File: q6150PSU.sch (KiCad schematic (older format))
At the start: 22 parts, among them P1 Vin, P2 Vout, Q1 Q_NMOS_GSD, T1 TRANSFO, U1 LM3478

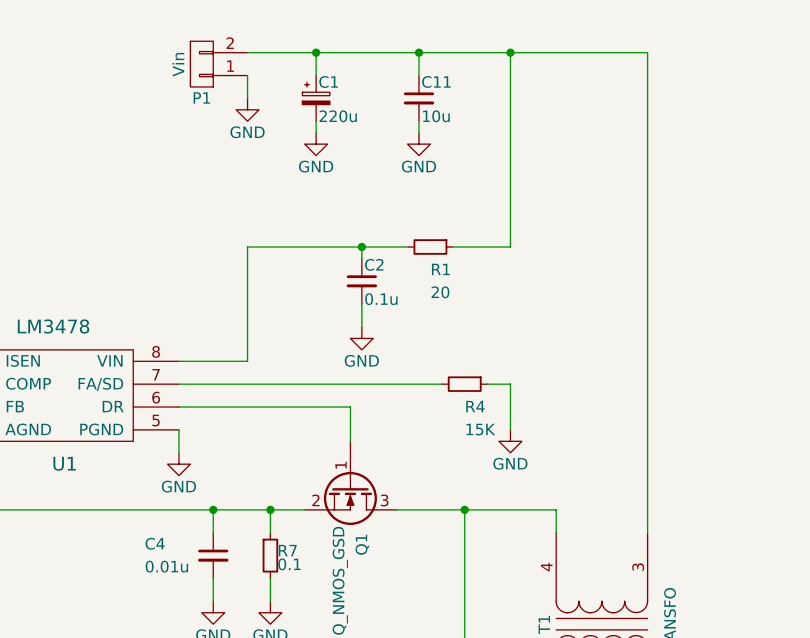
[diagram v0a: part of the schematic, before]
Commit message: All layout + Pot
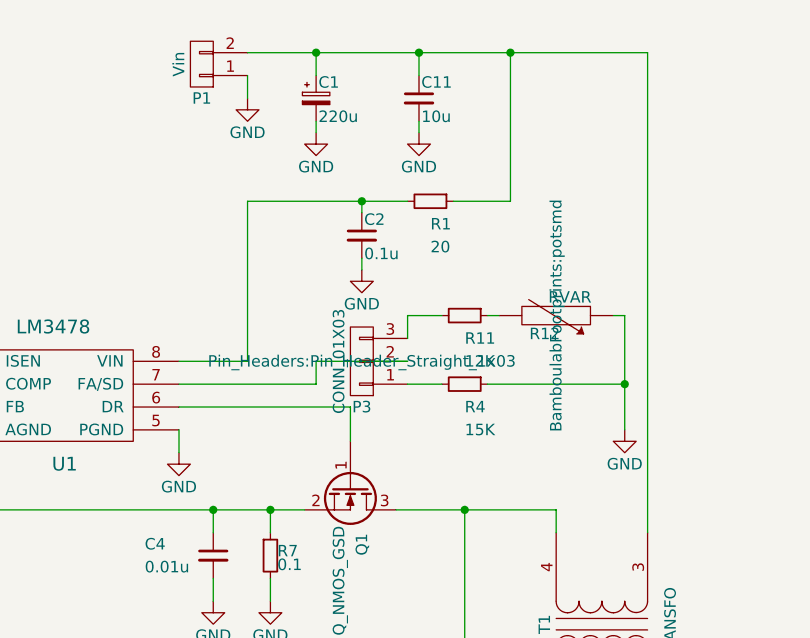
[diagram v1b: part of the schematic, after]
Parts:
- added P3: CONN_01X03, Pin_Headers:Pin_Header_Straight_1x03, symbol CONN_01X03
- added R11: 12K, Resistors_SMD:R_0805_HandSoldering, symbol R_Small
- added R12: RVAR, BamboulabFootprints:potsmd, symbol RVAR
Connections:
- net GND: now also R12.1
- net at U1.7 (FA/SD): now also P3.2 (P2); no longer R4.2
- new net: P3.1 (P1), R4.2
- new net: R11.1, R12.2
- new net: P3.3 (P3), R11.2
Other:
- moved on the sheet: C2, R1
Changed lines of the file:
@@
 L R_Small R1
 U 1 1 57F6A221
-P 5200 2750
-F 0 "R1" V 5300 2750 50  0000 L CNN
-F 1 "20" V 5400 2750 50  0000 L CNN
-F 2 "Resistors_SMD:R_0805_HandSoldering" H 5200 2750 50  0001 C CNN
-F 3 "" H 5200 2750 50  0000 C CNN
-	1    5200 2750
+P 5200 2550
+F 0 "R1" V 5300 2550 50  0000 L CNN
+F 1 "20" V 5400 2550 50  0000 L CNN
+F 2 "Resistors_SMD:R_0805_HandSoldering" H 5200 2550 50  0001 C CNN
+F 3 "" H 5200 2550 50  0000 C CNN
+	1    5200 2550
 	0    1    1    0
 $EndComp
@@
 L C_Small C2
 U 1 1 57F6A28E
-P 4900 2900
-F 0 "C2" H 4910 2970 50  0000 L CNN
-F 1 "0.1u" H 4910 2820 50  0000 L CNN
-F 2 "Capacitors_SMD:C_0805_HandSoldering" H 4900 2900 50  0001 C CNN
-F 3 "" H 4900 2900 50  0000 C CNN
-	1    4900 2900
+P 4900 2700
+F 0 "C2" H 4910 2770 50  0000 L CNN
+F 1 "0.1u" H 4910 2620 50  0000 L CNN
+F 2 "Capacitors_SMD:C_0805_HandSoldering" H 4900 2700 50  0001 C CNN
+F 3 "" H 4900 2700 50  0000 C CNN
+	1    4900 2700
 	1    0    0    -1
 $EndComp
@@
 L GND #PWR04
 U 1 1 57F6A2BF
-P 4900 3100
-F 0 "#PWR04" H 4900 2850 50  0001 C CNN
-F 1 "GND" H 4900 2950 50  0000 C CNN
-F 2 "" H 4900 3100 50  0000 C CNN
-F 3 "" H 4900 3100 50  0000 C CNN
-	1    4900 3100
+P 4900 2850
+F 0 "#PWR04" H 4900 2600 50  0001 C CNN
+F 1 "GND" H 4900 2700 50  0000 C CNN
+F 2 "" H 4900 2850 50  0000 C CNN
+F 3 "" H 4900 2850 50  0000 C CNN
+	1    4900 2850
 	1    0    0    -1
 $EndComp
@@
 	5150 2200 5150 2250
 Wire Wire Line
-	4900 3000 4900 3100
-Wire Wire Line
-	5300 2750 5550 2750
-Wire Wire Line
-	5550 2750 5550 1900
+	4900 2800 4900 2850
+Wire Wire Line
+	5300 2550 5550 2550
+Wire Wire Line
+	5550 2550 5550 1900
 Connection ~ 5150 1900
 Wire Wire Line
-	4400 2750 5100 2750
-Wire Wire Line
-	4900 2750 4900 2800
-Wire Wire Line
-	4400 2750 4400 3250
+	4400 2550 5100 2550
+Wire Wire Line
+	4900 2550 4900 2600
+Wire Wire Line
+	4400 2550 4400 3250
 Wire Wire Line
 	4400 3250 4100 3250
-Connection ~ 4900 2750
+Connection ~ 4900 2550
 Connection ~ 5550 1900
 Wire Wire Line
@@
 	3850 5050 3800 5050
 Wire Wire Line
-	4100 3350 5250 3350
+	5100 3350 5250 3350
 $Comp
 L GND #PWR015
 U 1 1 57F6FCA3
-P 5550 3550
-F 0 "#PWR015" H 5550 3300 50  0001 C CNN
-F 1 "GND" H 5550 3400 50  0000 C CNN
-F 2 "" H 5550 3550 50  0000 C CNN
-F 3 "" H 5550 3550 50  0000 C CNN
-	1    5550 3550
-	1    0    0    -1
-$EndComp
-Wire Wire Line
-	5450 3350 5550 3350
+P 6050 3550
+F 0 "#PWR015" H 6050 3300 50  0001 C CNN
+F 1 "GND" H 6050 3400 50  0000 C CNN
+F 2 "" H 6050 3550 50  0000 C CNN
+F 3 "" H 6050 3550 50  0000 C CNN
+	1    6050 3550
+	1    0    0    -1
+$EndComp
+Wire Wire Line
+	5450 3350 6050 3350
 Wire Wire Line
 	3600 5050 2700 5050
@@
 	6150 1900 6150 4000
 Wire Wire Line
-	5550 3350 5550 3550
+	6050 3050 6050 3550
+$Comp
+L R_Small R11
+U 1 1 58020BA0
+P 5350 3050
+F 0 "R11" V 5450 3050 50  0000 L CNN
+F 1 "12K" V 5550 3050 50  0000 L CNN
+F 2 "Resistors_SMD:R_0805_HandSoldering" H 5350 3050 50  0001 C CNN
+F 3 "" H 5350 3050 50  0000 C CNN
+	1    5350 3050
+	0    1    1    0
+$EndComp
+$Comp
+L RVAR R12
+U 1 1 58021FB9
+P 5750 3050
+F 0 "R12" V 5830 3000 50  0000 C CNN
+F 1 "RVAR" V 5670 3110 50  0000 C CNN
+F 2 "BamboulabFootprints:potsmd" H 5750 3050 50  0000 C CNN
+F 3 "" H 5750 3050 50  0000 C CNN
+	1    5750 3050
+	0    1    1    0
+$EndComp
+Wire Wire Line
+	5100 3050 5250 3050
+Wire Wire Line
+	5450 3050 5500 3050
+Wire Wire Line
+	6000 3050 6050 3050
+Connection ~ 6050 3350
+$Comp
+L CONN_01X03 P3
+U 1 1 58022C9D
+P 4900 3250
+F 0 "P3" H 4900 3450 50  0000 C CNN
+F 1 "CONN_01X03" V 5000 3250 50  0000 C CNN
+F 2 "Pin_Headers:Pin_Header_Straight_1x03" H 4900 3250 50  0000 C CNN
+F 3 "" H 4900 3250 50  0000 C CNN
+	1    4900 3250
+	-1   0    0    1
+$EndComp
+Wire Wire Line
+	5100 3150 5100 3050
+Wire Wire Line
+	4100 3350 4700 3350
+Wire Wire Line
+	4700 3350 4700 3250
+Wire Wire Line
+	4700 3250 5100 3250
 $EndSCHEMATC

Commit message: Fixed and it works!
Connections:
- net at C5.1, C6.1, D1.1 (K)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: now also R10.1
- net at D1.2 (A), T1.2 (AB): no longer R10.1
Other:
- moved on the sheet: C2, C7, D1, P3, R10, R11, R12, R4, R8, R9
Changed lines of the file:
@@
 L C_Small C2
 U 1 1 57F6A28E
-P 4900 2700
-F 0 "C2" H 4910 2770 50  0000 L CNN
-F 1 "0.1u" H 4910 2620 50  0000 L CNN
-F 2 "Capacitors_SMD:C_0805_HandSoldering" H 4900 2700 50  0001 C CNN
-F 3 "" H 4900 2700 50  0000 C CNN
-	1    4900 2700
+P 4800 2700
+F 0 "C2" H 4810 2770 50  0000 L CNN
+F 1 "0.1u" H 4810 2620 50  0000 L CNN
+F 2 "Capacitors_SMD:C_0805_HandSoldering" H 4800 2700 50  0001 C CNN
+F 3 "" H 4800 2700 50  0000 C CNN
+	1    4800 2700
 	1    0    0    -1
 $EndComp
@@
 L GND #PWR04
 U 1 1 57F6A2BF
-P 4900 2850
-F 0 "#PWR04" H 4900 2600 50  0001 C CNN
-F 1 "GND" H 4900 2700 50  0000 C CNN
-F 2 "" H 4900 2850 50  0000 C CNN
-F 3 "" H 4900 2850 50  0000 C CNN
-	1    4900 2850
+P 4800 2850
+F 0 "#PWR04" H 4800 2600 50  0001 C CNN
+F 1 "GND" H 4800 2700 50  0000 C CNN
+F 2 "" H 4800 2850 50  0000 C CNN
+F 3 "" H 4800 2850 50  0000 C CNN
+	1    4800 2850
 	1    0    0    -1
 $EndComp
@@
 L R_Small R4
 U 1 1 57F6BD03
-P 5350 3350
-F 0 "R4" V 5450 3350 50  0000 L CNN
-F 1 "15K" V 5550 3350 50  0000 L CNN
-F 2 "Resistors_SMD:R_0805_HandSoldering" H 5350 3350 50  0001 C CNN
-F 3 "" H 5350 3350 50  0000 C CNN
-	1    5350 3350
+P 5500 3350
+F 0 "R4" V 5600 3350 50  0000 L CNN
+F 1 "15K" V 5700 3350 50  0000 L CNN
+F 2 "Resistors_SMD:R_0805_HandSoldering" H 5500 3350 50  0001 C CNN
+F 3 "" H 5500 3350 50  0000 C CNN
+	1    5500 3350
 	0    1    1    0
 $EndComp
@@
 L D_Schottky_Small D1
 U 1 1 57F6D48D
-P 6450 5050
-F 0 "D1" H 6400 5130 50  0000 L CNN
-F 1 "STPS4S200" H 6170 4970 50  0000 L CNN
-F 2 "Diodes_SMD:SMB_Handsoldering" V 6450 5050 50  0001 C CNN
-F 3 "" V 6450 5050 50  0000 C CNN
-	1    6450 5050
+P 6350 5050
+F 0 "D1" H 6300 5130 50  0000 L CNN
+F 1 "STPS4S200" H 6070 4970 50  0000 L CNN
+F 2 "Diodes_SMD:SMB_Handsoldering" V 6350 5050 50  0001 C CNN
+F 3 "" V 6350 5050 50  0000 C CNN
+	1    6350 5050
 	-1   0    0    1
 $EndComp
@@
 L GND #PWR014
 U 1 1 57F6E467
-P 2700 5350
-F 0 "#PWR014" H 2700 5100 50  0001 C CNN
-F 1 "GND" H 2700 5200 50  0000 C CNN
-F 2 "" H 2700 5350 50  0000 C CNN
-F 3 "" H 2700 5350 50  0000 C CNN
-	1    2700 5350
+P 2700 5600
+F 0 "#PWR014" H 2700 5350 50  0001 C CNN
+F 1 "GND" H 2700 5450 50  0000 C CNN
+F 2 "" H 2700 5600 50  0000 C CNN
+F 3 "" H 2700 5600 50  0000 C CNN
+	1    2700 5600
 	1    0    0    -1
 $EndComp
@@
 L C_Small C7
 U 1 1 57F6E4A1
-P 2700 5200
-F 0 "C7" H 2710 5270 50  0000 L CNN
-F 1 "0.001" H 2710 5120 50  0000 L CNN
-F 2 "Capacitors_SMD:C_0805_HandSoldering" H 2700 5200 50  0001 C CNN
-F 3 "" H 2700 5200 50  0000 C CNN
-	1    2700 5200
+P 2700 5450
+F 0 "C7" H 2710 5520 50  0000 L CNN
+F 1 "0.001" H 2710 5370 50  0000 L CNN
+F 2 "Capacitors_SMD:C_0805_HandSoldering" H 2700 5450 50  0001 C CNN
+F 3 "" H 2700 5450 50  0000 C CNN
+	1    2700 5450
 	1    0    0    -1
 $EndComp
@@
 L R_Small R8
 U 1 1 57F6E5C7
-P 3700 5050
-F 0 "R8" H 3730 5070 50  0000 L CNN
-F 1 "1M" H 3730 5010 50  0000 L CNN
-F 2 "Resistors_SMD:R_0805_HandSoldering" H 3700 5050 50  0001 C CNN
-F 3 "" H 3700 5050 50  0000 C CNN
-	1    3700 5050
+P 3700 5300
+F 0 "R8" H 3730 5320 50  0000 L CNN
+F 1 "1M" H 3730 5260 50  0000 L CNN
+F 2 "Resistors_SMD:R_0805_HandSoldering" H 3700 5300 50  0001 C CNN
+F 3 "" H 3700 5300 50  0000 C CNN
+	1    3700 5300
 	0    1    1    0
 $EndComp
@@
 L R_Small R9
 U 1 1 57F6E6A8
-P 3950 5050
-F 0 "R9" H 3980 5070 50  0000 L CNN
-F 1 "820K" H 3980 5010 50  0000 L CNN
-F 2 "Resistors_SMD:R_0805_HandSoldering" H 3950 5050 50  0001 C CNN
-F 3 "" H 3950 5050 50  0000 C CNN
-	1    3950 5050
+P 3950 5300
+F 0 "R9" H 3980 5320 50  0000 L CNN
+F 1 "820K" H 3980 5260 50  0000 L CNN
+F 2 "Resistors_SMD:R_0805_HandSoldering" H 3950 5300 50  0001 C CNN
+F 3 "" H 3950 5300 50  0000 C CNN
+	1    3950 5300
 	0    1    1    0
 $EndComp
@@
 L R_Small R10
 U 1 1 57F6E6EB
-P 4200 5050
-F 0 "R10" H 4230 5070 50  0000 L CNN
-F 1 "24K" H 4230 5010 50  0000 L CNN
-F 2 "Resistors_SMD:R_0805_HandSoldering" H 4200 5050 50  0001 C CNN
-F 3 "" H 4200 5050 50  0000 C CNN
-	1    4200 5050
+P 4200 5300
+F 0 "R10" H 4230 5320 50  0000 L CNN
+F 1 "24K" H 4230 5260 50  0000 L CNN
+F 2 "Resistors_SMD:R_0805_HandSoldering" H 4200 5300 50  0001 C CNN
+F 3 "" H 4200 5300 50  0000 C CNN
+	1    4200 5300
 	0    1    1    0
 $EndComp
@@
 	5150 2200 5150 2250
 Wire Wire Line
-	4900 2800 4900 2850
+	4800 2800 4800 2850
 Wire Wire Line
 	5300 2550 5550 2550
@@
 	4400 2550 5100 2550
 Wire Wire Line
-	4900 2550 4900 2600
+	4800 2550 4800 2600
 Wire Wire Line
 	4400 2550 4400 3250
 Wire Wire Line
 	4400 3250 4100 3250
-Connection ~ 4900 2550
+Connection ~ 4800 2550
 Connection ~ 5550 1900
 Wire Wire Line
@@
 	6950 1900 6950 5100
 Wire Wire Line
-	6550 5050 6950 5050
-Wire Wire Line
-	4300 5050 6350 5050
+	6450 5050 6950 5050
+Wire Wire Line
+	6150 5050 6250 5050
 Wire Wire Line
 	7150 2000 7150 2100
@@
 Connection ~ 6600 5050
 Wire Wire Line
-	2700 3450 2700 5100
+	2700 3450 2700 5350
 Connection ~ 2700 3450
 Wire Wire Line
-	2700 5300 2700 5350
-Connection ~ 6150 5050
-Wire Wire Line
-	4100 5050 4050 5050
-Wire Wire Line
-	3850 5050 3800 5050
-Wire Wire Line
-	5100 3350 5250 3350
+	2700 5550 2700 5600
+Wire Wire Line
+	4100 5300 4050 5300
+Wire Wire Line
+	3850 5300 3800 5300
+Wire Wire Line
+	5250 3350 5400 3350
 $Comp
 L GND #PWR015
@@
 $EndComp
 Wire Wire Line
-	5450 3350 6050 3350
-Wire Wire Line
-	3600 5050 2700 5050
-Connection ~ 2700 5050
+	5600 3350 6050 3350
+Wire Wire Line
+	3600 5300 2700 5300
+Connection ~ 2700 5300
 Wire Wire Line
 	5750 3900 5750 4000
@@
 L R_Small R11
 U 1 1 58020BA0
-P 5350 3050
-F 0 "R11" V 5450 3050 50  0000 L CNN
-F 1 "12K" V 5550 3050 50  0000 L CNN
-F 2 "Resistors_SMD:R_0805_HandSoldering" H 5350 3050 50  0001 C CNN
-F 3 "" H 5350 3050 50  0000 C CNN
-	1    5350 3050
+P 5450 3050
+F 0 "R11" V 5550 3050 50  0000 L CNN
+F 1 "12K" V 5650 3050 50  0000 L CNN
+F 2 "Resistors_SMD:R_0805_HandSoldering" H 5450 3050 50  0001 C CNN
+F 3 "" H 5450 3050 50  0000 C CNN
+	1    5450 3050
 	0    1    1    0
 $EndComp
@@
 L RVAR R12
 U 1 1 58021FB9
-P 5750 3050
-F 0 "R12" V 5830 3000 50  0000 C CNN
-F 1 "RVAR" V 5670 3110 50  0000 C CNN
-F 2 "BamboulabFootprints:potsmd" H 5750 3050 50  0000 C CNN
-F 3 "" H 5750 3050 50  0000 C CNN
-	1    5750 3050
-	0    1    1    0
-$EndComp
-Wire Wire Line
-	5100 3050 5250 3050
-Wire Wire Line
-	5450 3050 5500 3050
-Wire Wire Line
-	6000 3050 6050 3050
+P 5800 3050
+F 0 "R12" V 5880 3000 50  0000 C CNN
+F 1 "RVAR" V 5720 3110 50  0000 C CNN
+F 2 "BamboulabFootprints:potsmd" H 5800 3050 50  0001 C CNN
+F 3 "" H 5800 3050 50  0000 C CNN
+	1    5800 3050
+	0    1    1    0
+$EndComp
+Wire Wire Line
+	5250 3050 5350 3050
+Wire Wire Line
+	5550 3050 5550 3050
 Connection ~ 6050 3350
 $Comp
 L CONN_01X03 P3
 U 1 1 58022C9D
-P 4900 3250
-F 0 "P3" H 4900 3450 50  0000 C CNN
-F 1 "CONN_01X03" V 5000 3250 50  0000 C CNN
-F 2 "Pin_Headers:Pin_Header_Straight_1x03" H 4900 3250 50  0000 C CNN
-F 3 "" H 4900 3250 50  0000 C CNN
-	1    4900 3250
+P 5050 3250
+F 0 "P3" H 5050 3450 50  0000 C CNN
+F 1 "CONN_01X03" V 5150 3250 50  0000 C CNN
+F 2 "Pin_Headers:Pin_Header_Straight_1x03" H 5050 3250 50  0001 C CNN
+F 3 "" H 5050 3250 50  0000 C CNN
+	1    5050 3250
 	-1   0    0    1
 $EndComp
 Wire Wire Line
-	5100 3150 5100 3050
+	5250 3150 5250 3050
 Wire Wire Line
 	4100 3350 4700 3350
@@
 	4700 3350 4700 3250
 Wire Wire Line
-	4700 3250 5100 3250
+	4700 3250 5250 3250
+Wire Wire Line
+	4300 5300 6500 5300
+Wire Wire Line
+	6500 5300 6500 5050
+Connection ~ 6500 5050
 $EndSCHEMATC
